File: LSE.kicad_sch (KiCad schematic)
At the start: 5 parts, among them Y2 32.758kHz

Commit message: ongoing add of MCU, etc.
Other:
- title: ADCs for 10K thermistors -> Multiplex I2C to Screw Terminal connectors
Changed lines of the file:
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@@
 	(paper "A4")
 	(title_block
-		(title "ADCs for 10K thermistors")
-		(date "2025-01-07")
-		(rev "v0.1.1")
+		(title "Multiplex I2C to Screw Terminal connectors")
+		(date "2025-09-07")
+		(rev "v0.2.0")
 	)
 	(junction
@@
 		(instances
 			(project "SensorProject_t16-pcb"
-				(path "/0c2d0c14-8850-4a30-bb78-b2f40cb442ba/f12d0b95-be3f-41e2-8b41-943aec5e1edf/349f89d2-b212-45c7-8a70-67b2942fde7b"
+				(path "/0c2d0c14-8850-4a30-bb78-b2f40cb442ba/2810e5bd-88e3-445e-9497-ea39bfab4c18/349f89d2-b212-45c7-8a70-67b2942fde7b"
 					(reference "C13")
 					(unit 1)
@@
 		(instances
 			(project "SensorProject_t16-pcb"
-				(path "/0c2d0c14-8850-4a30-bb78-b2f40cb442ba/f12d0b95-be3f-41e2-8b41-943aec5e1edf/349f89d2-b212-45c7-8a70-67b2942fde7b"
+				(path "/0c2d0c14-8850-4a30-bb78-b2f40cb442ba/2810e5bd-88e3-445e-9497-ea39bfab4c18/349f89d2-b212-45c7-8a70-67b2942fde7b"
 					(reference "C12")
 					(unit 1)
@@
 		(instances
 			(project ""
-				(path "/0c2d0c14-8850-4a30-bb78-b2f40cb442ba/f12d0b95-be3f-41e2-8b41-943aec5e1edf/349f89d2-b212-45c7-8a70-67b2942fde7b"
+				(path "/0c2d0c14-8850-4a30-bb78-b2f40cb442ba/2810e5bd-88e3-445e-9497-ea39bfab4c18/349f89d2-b212-45c7-8a70-67b2942fde7b"
 					(reference "NT2")
 					(unit 1)
@@
 		(instances
 			(project "SensorProject_t16-pcb"
-				(path "/0c2d0c14-8850-4a30-bb78-b2f40cb442ba/f12d0b95-be3f-41e2-8b41-943aec5e1edf/349f89d2-b212-45c7-8a70-67b2942fde7b"
+				(path "/0c2d0c14-8850-4a30-bb78-b2f40cb442ba/2810e5bd-88e3-445e-9497-ea39bfab4c18/349f89d2-b212-45c7-8a70-67b2942fde7b"
 					(reference "#PWR093")
 					(unit 1)
@@
 		(instances
 			(project "SensorProject_t16-pcb"
-				(path "/0c2d0c14-8850-4a30-bb78-b2f40cb442ba/f12d0b95-be3f-41e2-8b41-943aec5e1edf/349f89d2-b212-45c7-8a70-67b2942fde7b"
+				(path "/0c2d0c14-8850-4a30-bb78-b2f40cb442ba/2810e5bd-88e3-445e-9497-ea39bfab4c18/349f89d2-b212-45c7-8a70-67b2942fde7b"
 					(reference "R29")
 					(unit 1)
@@
 		(instances
 			(project ""
-				(path "/0c2d0c14-8850-4a30-bb78-b2f40cb442ba/f12d0b95-be3f-41e2-8b41-943aec5e1edf/349f89d2-b212-45c7-8a70-67b2942fde7b"
+				(path "/0c2d0c14-8850-4a30-bb78-b2f40cb442ba/2810e5bd-88e3-445e-9497-ea39bfab4c18/349f89d2-b212-45c7-8a70-67b2942fde7b"
 					(reference "#PWR062")
 					(unit 1)
@@
 		(instances
 			(project "SensorProject_t16-pcb"
-				(path "/0c2d0c14-8850-4a30-bb78-b2f40cb442ba/f12d0b95-be3f-41e2-8b41-943aec5e1edf/349f89d2-b212-45c7-8a70-67b2942fde7b"
+				(path "/0c2d0c14-8850-4a30-bb78-b2f40cb442ba/2810e5bd-88e3-445e-9497-ea39bfab4c18/349f89d2-b212-45c7-8a70-67b2942fde7b"
 					(reference "Y2")
 					(unit 1)

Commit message: symbols an footprints added for f411 change. ERC passes.
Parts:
- C12, C13: footprint ProjectLib:C_0402_1005Metric -> ProjectLib:C_0805_2012Metric
- R29: footprint ProjectLib:R_0402_1005Metric -> ProjectLib:R_0603_1608Metric
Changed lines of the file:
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@@
 			)
 		)
-		(property "Footprint" "ProjectLib:C_0402_1005Metric"
+		(property "Footprint" "ProjectLib:C_0805_2012Metric"
 			(at 128.5748 101.6 0)
 			(effects
@@
 			)
 		)
-		(property "Datasheet" ""
+		(property "Datasheet" "~"
 			(at 129.54 105.41 0)
 			(effects
@@
 			)
 		)
-		(property "Footprint" "ProjectLib:C_0402_1005Metric"
+		(property "Footprint" "ProjectLib:C_0805_2012Metric"
 			(at 112.0648 101.6 0)
 			(effects
@@
 			)
 		)
-		(property "Datasheet" ""
+		(property "Datasheet" "~"
 			(at 113.03 105.41 0)
 			(effects
@@
 			)
 		)
-		(property "Footprint" "ProjectLib:R_0402_1005Metric"
+		(property "Footprint" "ProjectLib:R_0603_1608Metric"
 			(at 130.556 85.344 90)
 			(effects
@@
 			)
 		)
-		(property "Datasheet" ""
+		(property "Datasheet" "~"
 			(at 129.54 85.09 0)
 			(effects
@@
 		(dnp no)
 		(fields_autoplaced yes)
-		(property "Reference" "#PWR062"
+		(property "Reference" "#PWR0110"
 			(at 113.03 125.73 0)
 			(effects
@@
 			(project ""
 				(path "/0c2d0c14-8850-4a30-bb78-b2f40cb442ba/2810e5bd-88e3-445e-9497-ea39bfab4c18/349f89d2-b212-45c7-8a70-67b2942fde7b"
-					(reference "#PWR062")
+					(reference "#PWR0110")
 					(unit 1)
 				)
@@
 			)
 		)
-		(property "Datasheet" "https://www.microcrystal.com/fileadmin/Media/Products/32kHz/Datasheet/CM9V-T1A.pdf"
+		(property "Datasheet" "~"
 			(at 120.65 95.25 0)
 			(effects
@@
 			)
 		)
-		(property "Description" "Two pin crystal, 7pF"
+		(property "Description" "Two pin crystal"
 			(at 120.65 95.25 0)
 			(effects

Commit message: ongoing
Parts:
- C12, C13: footprint ProjectLib:C_0805_2012Metric -> ProjectLib:C_0402_1005Metric
- R29: footprint ProjectLib:R_0603_1608Metric -> ProjectLib:R_0402_1005Metric
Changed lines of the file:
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@@
 			)
 		)
-		(property "Footprint" "ProjectLib:C_0805_2012Metric"
+		(property "Footprint" "ProjectLib:C_0402_1005Metric"
 			(at 128.5748 101.6 0)
 			(effects
@@
 			)
 		)
-		(property "Footprint" "ProjectLib:C_0805_2012Metric"
+		(property "Footprint" "ProjectLib:C_0402_1005Metric"
 			(at 112.0648 101.6 0)
 			(effects
@@
 			)
 		)
-		(property "Footprint" "ProjectLib:R_0603_1608Metric"
+		(property "Footprint" "ProjectLib:R_0402_1005Metric"
 			(at 130.556 85.344 90)
 			(effects

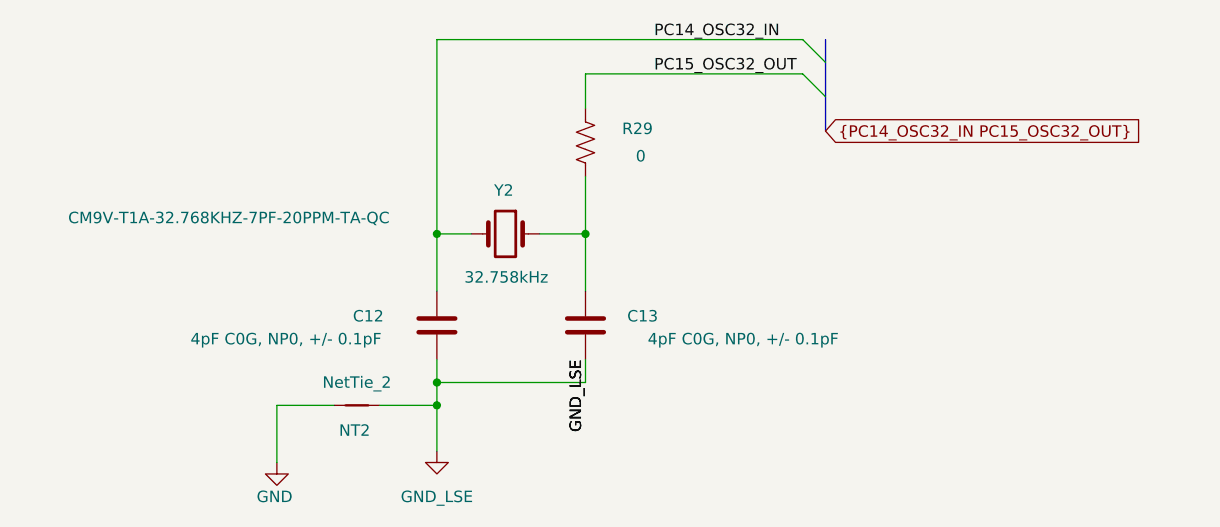
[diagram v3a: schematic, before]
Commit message: adding MCU, ongoing.
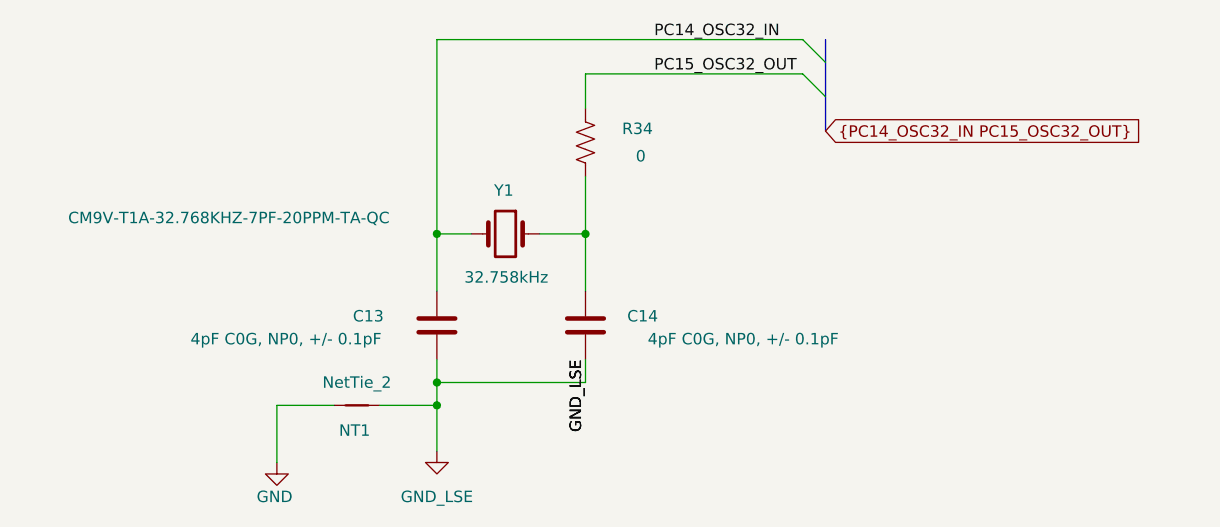
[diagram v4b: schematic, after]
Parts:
- renumbered C12 to C13, C13 to C14, NT2 to NT1, R29 to R34, Y2 to Y1
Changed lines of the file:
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@@
 		(on_board yes)
 		(dnp no)
-		(property "Reference" "C13"
+		(property "Reference" "C14"
 			(at 135.89 104.394 0)
 			(effects
@@
 			(project "SensorProject_t16-pcb"
 				(path "/0c2d0c14-8850-4a30-bb78-b2f40cb442ba/2810e5bd-88e3-445e-9497-ea39bfab4c18/349f89d2-b212-45c7-8a70-67b2942fde7b"
-					(reference "C13")
+					(reference "C14")
 					(unit 1)
 				)
@@
 		(on_board yes)
 		(dnp no)
-		(property "Reference" "C12"
+		(property "Reference" "C13"
 			(at 105.41 104.394 0)
 			(effects
@@
 			(project "SensorProject_t16-pcb"
 				(path "/0c2d0c14-8850-4a30-bb78-b2f40cb442ba/2810e5bd-88e3-445e-9497-ea39bfab4c18/349f89d2-b212-45c7-8a70-67b2942fde7b"
-					(reference "C12")
+					(reference "C13")
 					(unit 1)
 				)
@@
 		(on_board yes)
 		(dnp no)
-		(property "Reference" "NT2"
+		(property "Reference" "NT1"
 			(at 103.886 117.094 0)
 			(effects
@@
 			(project ""
 				(path "/0c2d0c14-8850-4a30-bb78-b2f40cb442ba/2810e5bd-88e3-445e-9497-ea39bfab4c18/349f89d2-b212-45c7-8a70-67b2942fde7b"
-					(reference "NT2")
+					(reference "NT1")
 					(unit 1)
 				)
@@
 		(on_board yes)
 		(dnp no)
-		(property "Reference" "#PWR093"
+		(property "Reference" "#PWR065"
 			(at 95.25 127 0)
 			(effects
@@
 			(project "SensorProject_t16-pcb"
 				(path "/0c2d0c14-8850-4a30-bb78-b2f40cb442ba/2810e5bd-88e3-445e-9497-ea39bfab4c18/349f89d2-b212-45c7-8a70-67b2942fde7b"
-					(reference "#PWR093")
+					(reference "#PWR065")
 					(unit 1)
 				)
@@
 		(on_board yes)
 		(dnp no)
-		(property "Reference" "R29"
+		(property "Reference" "R34"
 			(at 133.604 83.566 0)
 			(effects
@@
 			(project "SensorProject_t16-pcb"
 				(path "/0c2d0c14-8850-4a30-bb78-b2f40cb442ba/2810e5bd-88e3-445e-9497-ea39bfab4c18/349f89d2-b212-45c7-8a70-67b2942fde7b"
-					(reference "R29")
+					(reference "R34")
 					(unit 1)
 				)
@@
 		(dnp no)
 		(fields_autoplaced yes)
-		(property "Reference" "#PWR0110"
+		(property "Reference" "#PWR066"
 			(at 113.03 125.73 0)
 			(effects
@@
 			(project ""
 				(path "/0c2d0c14-8850-4a30-bb78-b2f40cb442ba/2810e5bd-88e3-445e-9497-ea39bfab4c18/349f89d2-b212-45c7-8a70-67b2942fde7b"
-					(reference "#PWR0110")
+					(reference "#PWR066")
 					(unit 1)
 				)
@@
 		(on_board yes)
 		(dnp no)
-		(property "Reference" "Y2"
+		(property "Reference" "Y1"
 			(at 119.38 90.424 0)
 			(effects
@@
 			(project "SensorProject_t16-pcb"
 				(path "/0c2d0c14-8850-4a30-bb78-b2f40cb442ba/2810e5bd-88e3-445e-9497-ea39bfab4c18/349f89d2-b212-45c7-8a70-67b2942fde7b"
-					(reference "Y2")
+					(reference "Y1")
 					(unit 1)
 				)

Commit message: ongoing.
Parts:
- renumbered C14 to C?, C13 to C?, NT1 to NT?, R34 to R?, Y1 to Y?
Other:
- title: Multiplex I2C to Screw Terminal connectors -> LSE
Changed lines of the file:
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@@
 	(paper "A4")
 	(title_block
-		(title "Multiplex I2C to Screw Terminal connectors")
-		(date "2025-09-07")
-		(rev "v0.2.0")
+		(title "LSE")
+		(date "2025-09-15")
+		(rev "v0.2.2")
 	)
 	(junction
@@
 		(on_board yes)
 		(dnp no)
-		(property "Reference" "C14"
+		(property "Reference" "C?"
 			(at 135.89 104.394 0)
 			(effects
@@
 			)
 		)
-		(property "Datasheet" "~"
+		(property "Datasheet" ""
 			(at 129.54 105.41 0)
 			(effects
@@
 		)
 		(instances
-			(project "SensorProject_t16-pcb"
+			(project "multiplexI2C"
 				(path "/0c2d0c14-8850-4a30-bb78-b2f40cb442ba/2810e5bd-88e3-445e-9497-ea39bfab4c18/349f89d2-b212-45c7-8a70-67b2942fde7b"
-					(reference "C14")
+					(reference "C?")
 					(unit 1)
 				)
@@
 		(on_board yes)
 		(dnp no)
-		(property "Reference" "C13"
+		(property "Reference" "C?"
 			(at 105.41 104.394 0)
 			(effects
@@
 			)
 		)
-		(property "Datasheet" "~"
+		(property "Datasheet" ""
 			(at 113.03 105.41 0)
 			(effects
@@
 		)
 		(instances
-			(project "SensorProject_t16-pcb"
+			(project "multiplexI2C"
 				(path "/0c2d0c14-8850-4a30-bb78-b2f40cb442ba/2810e5bd-88e3-445e-9497-ea39bfab4c18/349f89d2-b212-45c7-8a70-67b2942fde7b"
-					(reference "C13")
+					(reference "C?")
 					(unit 1)
 				)
@@
 		(on_board yes)
 		(dnp no)
-		(property "Reference" "NT1"
+		(property "Reference" "NT?"
 			(at 103.886 117.094 0)
 			(effects
@@
 		)
 		(instances
-			(project ""
+			(project "multiplexI2C"
 				(path "/0c2d0c14-8850-4a30-bb78-b2f40cb442ba/2810e5bd-88e3-445e-9497-ea39bfab4c18/349f89d2-b212-45c7-8a70-67b2942fde7b"
-					(reference "NT1")
+					(reference "NT?")
 					(unit 1)
 				)
@@
 		(on_board yes)
 		(dnp no)
-		(property "Reference" "#PWR065"
+		(property "Reference" "#PWR?"
 			(at 95.25 127 0)
 			(effects
@@
 		)
 		(instances
-			(project "SensorProject_t16-pcb"
+			(project "multiplexI2C"
 				(path "/0c2d0c14-8850-4a30-bb78-b2f40cb442ba/2810e5bd-88e3-445e-9497-ea39bfab4c18/349f89d2-b212-45c7-8a70-67b2942fde7b"
-					(reference "#PWR065")
+					(reference "#PWR?")
 					(unit 1)
 				)
@@
 		(on_board yes)
 		(dnp no)
-		(property "Reference" "R34"
+		(property "Reference" "R?"
 			(at 133.604 83.566 0)
 			(effects
@@
 			)
 		)
-		(property "Datasheet" "~"
+		(property "Datasheet" ""
 			(at 129.54 85.09 0)
 			(effects
@@
 		)
 		(instances
-			(project "SensorProject_t16-pcb"
+			(project "multiplexI2C"
 				(path "/0c2d0c14-8850-4a30-bb78-b2f40cb442ba/2810e5bd-88e3-445e-9497-ea39bfab4c18/349f89d2-b212-45c7-8a70-67b2942fde7b"
-					(reference "R34")
+					(reference "R?")
 					(unit 1)
 				)
@@
 		(dnp no)
 		(fields_autoplaced yes)
-		(property "Reference" "#PWR066"
+		(property "Reference" "#PWR?"
 			(at 113.03 125.73 0)
 			(effects
@@
 		)
 		(instances
-			(project ""
+			(project "multiplexI2C"
 				(path "/0c2d0c14-8850-4a30-bb78-b2f40cb442ba/2810e5bd-88e3-445e-9497-ea39bfab4c18/349f89d2-b212-45c7-8a70-67b2942fde7b"
-					(reference "#PWR066")
+					(reference "#PWR?")
 					(unit 1)
 				)
@@
 		(on_board yes)
 		(dnp no)
-		(property "Reference" "Y1"
+		(property "Reference" "Y?"
 			(at 119.38 90.424 0)
 			(effects
@@
 			)
 		)
-		(property "Datasheet" "~"
+		(property "Datasheet" "https://www.microcrystal.com/fileadmin/Media/Products/32kHz/Datasheet/CM9V-T1A.pdf"
 			(at 120.65 95.25 0)
 			(effects
@@
 			)
 		)
-		(property "Description" "Two pin crystal"
+		(property "Description" "Two pin crystal, 7pF"
 			(at 120.65 95.25 0)
 			(effects
@@
 		)
 		(instances
-			(project "SensorProject_t16-pcb"
+			(project "multiplexI2C"
 				(path "/0c2d0c14-8850-4a30-bb78-b2f40cb442ba/2810e5bd-88e3-445e-9497-ea39bfab4c18/349f89d2-b212-45c7-8a70-67b2942fde7b"
-					(reference "Y1")
+					(reference "Y?")
 					(unit 1)
 				)

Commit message: ongoing.
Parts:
- gave numbers to parts that had none: 5
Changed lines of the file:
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@@
 		(on_board yes)
 		(dnp no)
-		(property "Reference" "C?"
+		(property "Reference" "C502"
 			(at 135.89 104.394 0)
 			(effects
@@
 			(project "multiplexI2C"
 				(path "/0c2d0c14-8850-4a30-bb78-b2f40cb442ba/2810e5bd-88e3-445e-9497-ea39bfab4c18/349f89d2-b212-45c7-8a70-67b2942fde7b"
-					(reference "C?")
+					(reference "C502")
 					(unit 1)
 				)
@@
 		(on_board yes)
 		(dnp no)
-		(property "Reference" "C?"
+		(property "Reference" "C501"
 			(at 105.41 104.394 0)
 			(effects
@@
 			(project "multiplexI2C"
 				(path "/0c2d0c14-8850-4a30-bb78-b2f40cb442ba/2810e5bd-88e3-445e-9497-ea39bfab4c18/349f89d2-b212-45c7-8a70-67b2942fde7b"
-					(reference "C?")
+					(reference "C501")
 					(unit 1)
 				)
@@
 		(on_board yes)
 		(dnp no)
-		(property "Reference" "NT?"
+		(property "Reference" "NT501"
 			(at 103.886 117.094 0)
 			(effects
@@
 			(project "multiplexI2C"
 				(path "/0c2d0c14-8850-4a30-bb78-b2f40cb442ba/2810e5bd-88e3-445e-9497-ea39bfab4c18/349f89d2-b212-45c7-8a70-67b2942fde7b"
-					(reference "NT?")
+					(reference "NT501")
 					(unit 1)
 				)
@@
 		(on_board yes)
 		(dnp no)
-		(property "Reference" "#PWR?"
+		(property "Reference" "#PWR0502"
 			(at 95.25 127 0)
 			(effects
@@
 			(project "multiplexI2C"
 				(path "/0c2d0c14-8850-4a30-bb78-b2f40cb442ba/2810e5bd-88e3-445e-9497-ea39bfab4c18/349f89d2-b212-45c7-8a70-67b2942fde7b"
-					(reference "#PWR?")
+					(reference "#PWR0502")
 					(unit 1)
 				)
@@
 		(on_board yes)
 		(dnp no)
-		(property "Reference" "R?"
+		(property "Reference" "R501"
 			(at 133.604 83.566 0)
 			(effects
@@
 			(project "multiplexI2C"
 				(path "/0c2d0c14-8850-4a30-bb78-b2f40cb442ba/2810e5bd-88e3-445e-9497-ea39bfab4c18/349f89d2-b212-45c7-8a70-67b2942fde7b"
-					(reference "R?")
+					(reference "R501")
 					(unit 1)
 				)
@@
 		(dnp no)
 		(fields_autoplaced yes)
-		(property "Reference" "#PWR?"
+		(property "Reference" "#PWR0501"
 			(at 113.03 125.73 0)
 			(effects
@@
 			(project "multiplexI2C"
 				(path "/0c2d0c14-8850-4a30-bb78-b2f40cb442ba/2810e5bd-88e3-445e-9497-ea39bfab4c18/349f89d2-b212-45c7-8a70-67b2942fde7b"
-					(reference "#PWR?")
+					(reference "#PWR0501")
 					(unit 1)
 				)
@@
 		(on_board yes)
 		(dnp no)
-		(property "Reference" "Y?"
+		(property "Reference" "Y501"
 			(at 119.38 90.424 0)
 			(effects
@@
 			(project "multiplexI2C"
 				(path "/0c2d0c14-8850-4a30-bb78-b2f40cb442ba/2810e5bd-88e3-445e-9497-ea39bfab4c18/349f89d2-b212-45c7-8a70-67b2942fde7b"
-					(reference "Y?")
+					(reference "Y501")
 					(unit 1)
 				)
